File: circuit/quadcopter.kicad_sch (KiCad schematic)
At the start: 110 parts, among them J1 Conn_01x01_Female, J10 Conn_01x01_Female, J13 Conn_01x01_Female, J15 Conn_01x01_Female, J16 Conn_01x01_Female, J17 Conn_01x01_Female, J18 USB_C_Receptacle_USB2.0, J19 Conn_01x08_Male, J2 Conn_01x01_Female, J21 Conn_01x01_Female, J22 Conn_01x01_Female, J23 Conn_01x01_Female, J24 Conn_01x01_Female, J25 Conn_01x01_Female, J26 Conn_01x01_Female, J28 Conn_01x01_Female, J29 Conn_01x01_Female, J3 Conn_01x01_Female, J30 Conn_01x01_Female, J31 Conn_01x01_Female, J32 Conn_01x01_Female, J33 Conn_01x01_Female, J34 Conn_01x01_Female, J37 Conn_01x01_Female, J4 Conn_01x01_Female, J40 Conn_01x01_Female, J41 Conn_01x01_Female, J42 Conn_01x01_Female, J43 Conn_01x01_Female, J44 Conn_01x01_Female, J45 Conn_01x01_Female, J46 Conn_01x01_Female, J47 Conn_01x01_Female, J48 Conn_01x01_Female, J49 Conn_01x01_Female, J5 Conn_Coaxial, J50 Conn_01x01_Female, J6 Conn_01x06_Male, J7 Conn_01x01_Female, J8 Conn_01x01_Female, J9 Conn_01x01_Female, Q1 AO3400A, SW1 SW_DIP_x01, U1 STM32G431CBU6, U2 ICM-42605, U3 DPS310, U4 3V3, U5 5V out, 30V max, U6 2450FM07D0034T, U7 W25Q80DVUXIE TR, U8 SX1281, Y1 16M, Y2 52Mhz, 12pF

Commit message: More work on routing
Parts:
- U7: value W25Q80DVUXIE TR -> W25Q80DVUXIE TR (16M)
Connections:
- net +3V3: no longer C19.2, C26.1, C28.2, L3.1, U8.1 (VR_PA), U8.2 (VDD_IN)
- net V_DCC: now also C26.1, C28.2, L3.1, U8.2 (VDD_IN)
- new net: C19.2, U8.1 (VR_PA)
- no-connect marks 7 -> 9
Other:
- note added: "10v reg for cam and vtx? Would allow for 8S batteries, if you also up max voltage on a few other parts"
- note added: "Example full buzzer circuit. Not on PCB or BOM."
- note added: "SWD connections for ST-Link debugging and flashing"
- note added: "Todo: TVS diode across battery?"
- note removed: "10v reg for cam and vtx?"
- note removed: "Example full buzzer circuit. Not on BOM!"
- note removed: "todo: Higher capacity flash"
- moved on the sheet: C2, C23, C5, J16, J17, J32, J33, J40, J41, J42, J43, J44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

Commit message: Power section redid, including 10v reg added
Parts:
- removed U5: 5V out, 30V max, Package_TO_SOT_SMD:SOT-89-3, symbol Regulator_Linear:HT75xx-1-SOT89
- added C20: 22uF 25V, Capacitor_SMD:C_0805_2012Metric, symbol Device:C
- added C21: 10nF 50V, Capacitor_SMD:C_0402_1005Metric, symbol Device:C
- added C22: 2.2u, Capacitor_SMD:C_0402_1005Metric, symbol Device:C
- added D4: SOD24-7 26V breakdown, Diode_SMD:D_SOD-323, symbol Device:D
- added D5: 40v 1A B5819WS, Diode_SMD:D_SOD-323, symbol Device:D
- added L4: 22u 900mA, Anyleaf_Shared:SMNR4020 inductor, symbol Device:L
- added R7: 3.3K, Resistor_SMD:R_0402_1005Metric, symbol Device:R
- added R8: 300, Resistor_SMD:R_0402_1005Metric, symbol Device:R
- added U5: EUP3458 1.2A, 30V max input, adj output, Package_TO_SOT_SMD:TSOT-23-6, symbol Regulator_Switching:AAT1217ICA-1.2
- added U9: 5v, 500mA, Package_TO_SOT_SMD:TSOT-23-5, symbol water_monitor-rescue:MCP1802-3.3-Anyleaf_shared
- C15: value 10uF 10V -> 1u 50V; LCSC C19702 -> C15849
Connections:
- net +5V: now also D5.1 (K); no longer D2.1 (K)
- net +BATT: now also D4.1 (K), U5.4 (EN), U5.5 (IN); no longer C27.2, J25.1 (Pin_1), J6.6 (Pin_6), L2.2
- net BAT_IN: now also D4.2 (A); no longer L2.1
- net GND: now also D2.2 (A), C20.2, C22.1, R8.1, U5.2 (GND), U9.2 (GND)
- net +10V: now reaches C15.2
- net +10V: now also J25.1 (Pin_1), J6.6 (Pin_6), C20.1, L4.1, R7.2, U9.1 (VIN), U9.3 (~{SHDN}); no longer D2.2 (A)
- new net: C21.1, U5.1 (BS)
- new net: C21.2, D2.1 (K), L4.2, U5.6 (SW)
- new net: C22.2, C27.2, L2.1, U9.5 (VOUT)
- new net: D5.2 (A), L2.2
- new net: R7.1, R8.2, U5.3 (FB)
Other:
- note added: "3.3k and 300 lead to 9.6V output"
- note added: "Analog filtering on the 5V line. We can use a smaller inductor here, than if it were on the 10k line that needs to handle current to the cam/Vtx"
- note added: "Calculated inductor value, for 25.2v in, 9.6vout, 30% ripple, and 1A current: 16.5uH"
- note added: "Note: Voltage range of CADDX vista DJI: 7.4 - 26.4V HDzero: Racev2: 7-26V Hdzero freestyle: 7-17V"
- note added: "See regulator DS for info on how to set resistances and capacitances"
- note added: "TVS diode to block transient voltage spikes"
- note added: "Using Diatone pinout, since it's perhaps the most popular (2022) Note that this places the battery line next to the signal pins; Batt -> Gnd -> current/uart -> motor may be a better layout."
- note added: "V_out = 0.8V * (R1 + R2)/R2"
- note added: "todo: Bigger flash, on back side?"
- note removed: "10v reg for cam and vtx? Would allow for 8S batteries, if you also up max voltage on a few other parts"
- note removed: "Battery cicrcuit that includes a LC lowpass filter, to reduce noise from the ESC."
- note removed: "Note: Voltage range of CADDX vista DJI: 7.4 - 26.4V HDzero: Racev2: 7-26V Hdzero freestyle: 7-17V max (4S!)"
- note removed: "See https://github.com/ExpressLRS/ExpressLRS-Hardware/tree/master/PCB/2400MHz/RX_Nano for a ELRS example"
- note removed: "Todo: TVS diode across battery?"
- note removed: "Using Diatone pinout, since it's perhaps the most popular (2022)"
- note removed: "todo: Check max v on inductor"
- moved on the sheet: C14, C27, C7, C8, D2, D3, J10, J13, J19, J21, J22, J23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

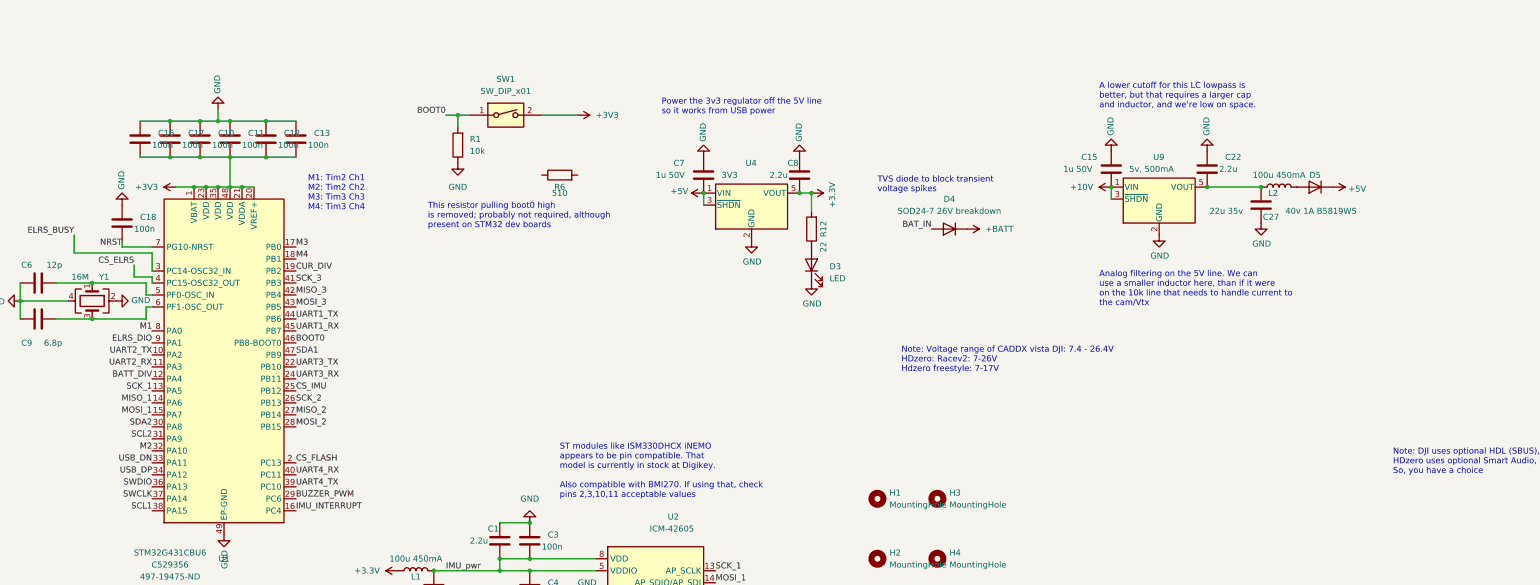
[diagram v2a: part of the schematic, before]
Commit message: More work on translating ELRS receiver code
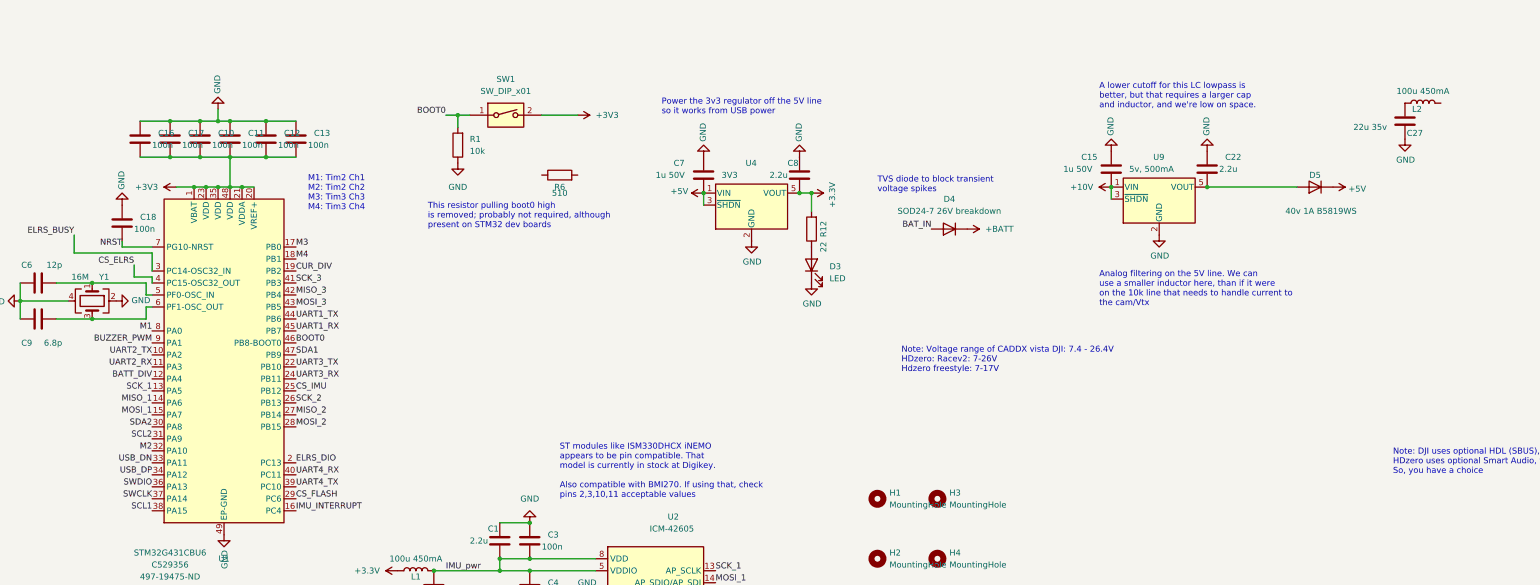
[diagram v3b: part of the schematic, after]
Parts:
- C27, L2: now left out of the parts list
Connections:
- net BUZZER_PWM: now also U1.9 (PA1); no longer U1.29 (PC6)
- net CS_FLASH: now also U1.29 (PC6); no longer U1.2 (PC13)
- net ELRS_DIO: now also U1.2 (PC13); no longer U1.9 (PA1)
- net at C22.2, U9.5 (VOUT): now also D5.2 (A); no longer C27.2, L2.1
- net at L2.2: no longer D5.2 (A)
- new net: C27.2, L2.1
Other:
- moved on the sheet: C27, L2
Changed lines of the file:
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@@
   (junction (at 54.61 336.55) (diameter 0) (color 0 0 0 0)
   )
-  (junction (at 347.98 48.26) (diameter 0) (color 0 0 0 0)
-  )
   (junction (at 193.04 129.54) (diameter 0) (color 0 0 0 0)
   )
@@
     (stroke (width 0) (type default) (color 0 0 0 0))
   )
-  (wire (pts (xy 336.55 48.26) (xy 347.98 48.26))
+  (wire (pts (xy 336.55 48.26) (xy 355.6 48.26))
     (stroke (width 0) (type default) (color 0 0 0 0))
   )
@@
     (effects (font (size 1.27 1.27)) (justify left bottom))
   )
-  (label "BUZZER_PWM" (at 143.51 114.3 0)
-    (effects (font (size 1.27 1.27)) (justify left bottom))
+  (label "BUZZER_PWM" (at 113.03 81.28 180)
+    (effects (font (size 1.27 1.27)) (justify right bottom))
   )
   (label "MOSI_3" (at 78.74 303.53 0)
@@
     (effects (font (size 1.27 1.27)) (justify right bottom))
   )
-  (label "CS_FLASH" (at 143.51 106.68 0)
+  (label "CS_FLASH" (at 143.51 114.3 0)
     (effects (font (size 1.27 1.27)) (justify left bottom))
   )
@@
     (effects (font (size 1.27 1.27)) (justify left bottom))
   )
-  (label "ELRS_DIO" (at 113.03 81.28 180)
-    (effects (font (size 1.27 1.27)) (justify right bottom))
+  (label "ELRS_DIO" (at 143.51 106.68 0)
+    (effects (font (size 1.27 1.27)) (justify left bottom))
   )
   (label "CS_ELRS" (at 109.22 64.77 180)
@@
     (pin "1")
   )
-  (symbol (lib_id "power:GND") (at 347.98 55.88 0) (unit 1)
+  (symbol (lib_id "power:GND") (at 378.46 38.1 0) (unit 1)
     (in_bom yes) (on_board yes)
-    (property "Reference" "#PWR?" (id 0) (at 347.98 62.23 0)
+    (property "Reference" "#PWR0125" (id 0) (at 378.46 44.45 0)
       (effects (font (size 1.27 1.27)) hide)
     )
-    (property "Value" "GND" (id 1) (at 348.107 60.2742 0))
-    (property "Footprint" "" (id 2) (at 347.98 55.88 0)
+    (property "Value" "GND" (id 1) (at 378.587 42.4942 0))
+    (property "Footprint" "" (id 2) (at 378.46 38.1 0)
       (effects (font (size 1.27 1.27)) hide)
     )
-    (property "Datasheet" "" (id 3) (at 347.98 55.88 0)
+    (property "Datasheet" "" (id 3) (at 378.46 38.1 0)
       (effects (font (size 1.27 1.27)) hide)
     )
@@
     (pin "2")
   )
-  (symbol (lib_id "Device:L") (at 351.79 48.26 90) (unit 1)
-    (in_bom yes) (on_board yes)
-    (property "Reference" "L2" (id 0) (at 350.52 49.53 90))
-    (property "Value" "100u 450mA" (id 1) (at 351.79 45.72 90))
-    (property "Footprint" "Anyleaf_Shared:SMNR4020 inductor" (id 2) (at 351.79 48.26 0)
+  (symbol (lib_id "Device:L") (at 382.27 30.48 90) (unit 1)
+    (in_bom no) (on_board no)
+    (property "Reference" "L2" (id 0) (at 381 31.75 90))
+    (property "Value" "100u 450mA" (id 1) (at 382.27 27.94 90))
+    (property "Footprint" "Anyleaf_Shared:SMNR4020 inductor" (id 2) (at 382.27 30.48 0)
       (effects (font (size 1.27 1.27)) hide)
     )
-    (property "Datasheet" "~" (id 3) (at 351.79 48.26 0)
+    (property "Datasheet" "~" (id 3) (at 382.27 30.48 0)
       (effects (font (size 1.27 1.27)) hide)
     )
-    (property "LCSC" "C467068" (id 4) (at 351.79 48.26 90)
+    (property "LCSC" "C467068" (id 4) (at 382.27 30.48 90)
       (effects (font (size 1.27 1.27)) hide)
     )
@@
     (pin "2")
   )
-  (symbol (lib_id "Device:C") (at 347.98 52.07 180) (unit 1)
-    (in_bom yes) (on_board yes)
-    (property "Reference" "C27" (id 0) (at 351.79 54.61 0)
+  (symbol (lib_id "Device:C") (at 378.46 34.29 180) (unit 1)
+    (in_bom no) (on_board no)
+    (property "Reference" "C27" (id 0) (at 382.27 36.83 0)
       (effects (font (size 1.27 1.27)) (justify left))
     )
-    (property "Value" "22u 35v" (id 1) (at 344.17 53.34 0)
+    (property "Value" "22u 35v" (id 1) (at 374.65 35.56 0)
       (effects (font (size 1.27 1.27)) (justify left))
     )
-    (property "Footprint" "Capacitor_SMD:C_0805_2012Metric" (id 2) (at 347.0148 48.26 0)
+    (property "Footprint" "Capacitor_SMD:C_0805_2012Metric" (id 2) (at 377.4948 30.48 0)
       (effects (font (size 1.27 1.27)) hide)
     )
-    (property "Datasheet" "~" (id 3) (at 347.98 52.07 0)
+    (property "Datasheet" "~" (id 3) (at 378.46 34.29 0)
       (effects (font (size 1.27 1.27)) hide)
     )
-    (property "LCSC" "C338080" (id 4) (at 347.98 52.07 0)
+    (property "LCSC" "C338080" (id 4) (at 378.46 34.29 0)
       (effects (font (size 1.27 1.27)) hide)
     )
@@
       (reference "#PWR0124") (unit 1) (value "GND") (footprint "")
     )
+    (path "/4cd6c931-bf25-4c72-8d1d-bb9bbbcd4add"
+      (reference "#PWR0125") (unit 1) (value "GND") (footprint "")
+    )
     (path "/76e20596-6bdb-42cd-a1dc-9b44805b2ea2"
       (reference "#PWR0126") (unit 1) (value "GND") (footprint "")
@@
       (reference "#PWR0180") (unit 1) (value "GND") (footprint "")
     )
-    (path "/4cd6c931-bf25-4c72-8d1d-bb9bbbcd4add"
-      (reference "#PWR?") (unit 1) (value "GND") (footprint "")
-    )
     (path "/4392ec2f-3eec-47ea-978d-f1725d990b74"

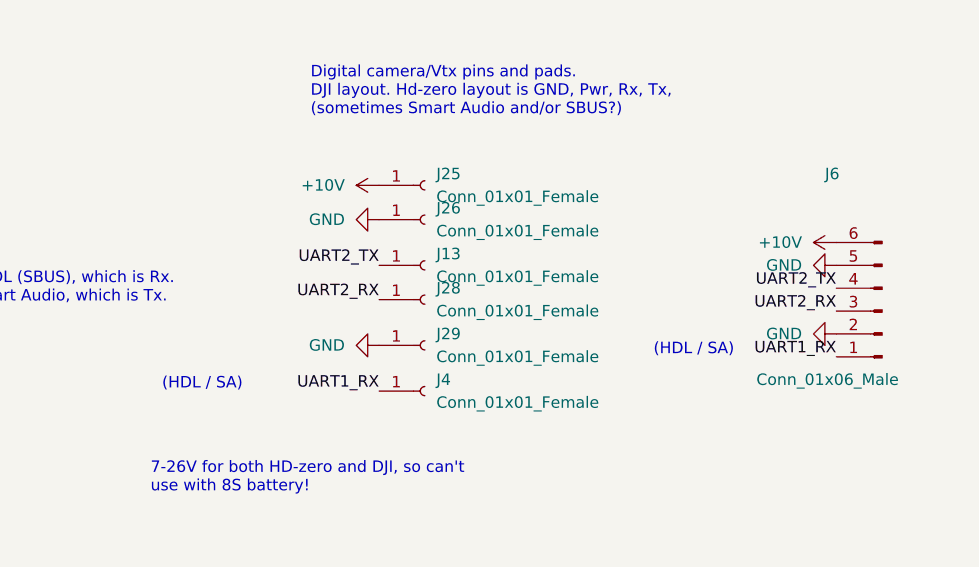
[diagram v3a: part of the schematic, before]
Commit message: Added list of ESC and VtX pinouts. Tweaks to IMU dma code
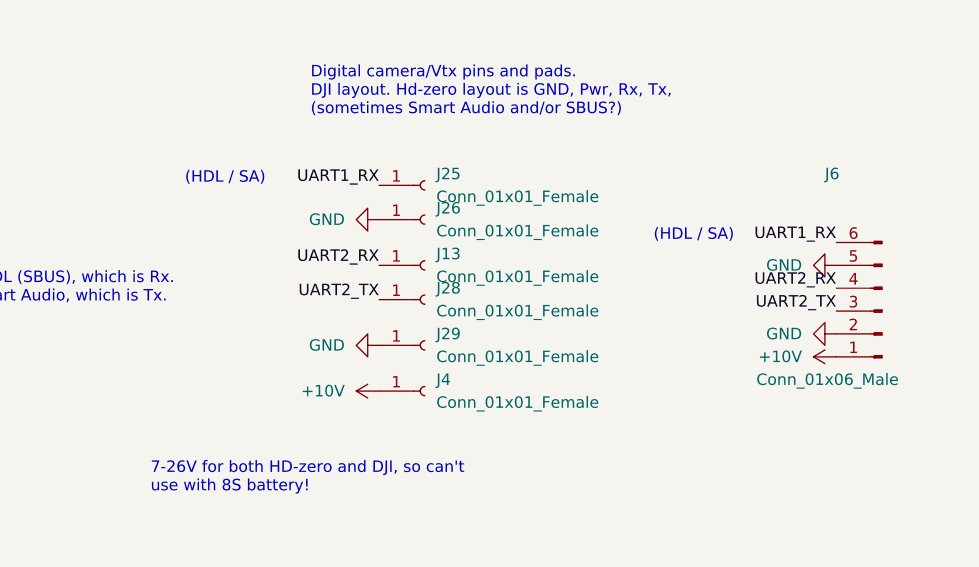
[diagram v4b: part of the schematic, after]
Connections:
- net +10V: now also J4.1 (Pin_1), J6.1 (Pin_1); no longer J25.1 (Pin_1), J6.6 (Pin_6)
- net UART1_RX: now also J25.1 (Pin_1), J6.6 (Pin_6); no longer J4.1 (Pin_1), J6.1 (Pin_1)
- net UART2_RX: now also J13.1 (Pin_1), J6.4 (Pin_4); no longer J28.1 (Pin_1), J6.3 (Pin_3)
- net UART2_TX: now also J28.1 (Pin_1), J6.3 (Pin_3); no longer J13.1 (Pin_1), J6.4 (Pin_4)
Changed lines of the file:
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@@
     (stroke (width 0) (type default) (color 0 0 0 0))
   )
-  (text "(HDL / SA)" (at 471.17 113.03 0)
+  (text "(HDL / SA)" (at 471.17 100.33 0)
     (effects (font (size 1.27 1.27)) (justify left bottom))
   )
@@
     (effects (font (size 1.27 1.27)) (justify left bottom))
   )
-  (text "(HDL / SA)" (at 416.56 116.84 0)
+  (text "(HDL / SA)" (at 419.1 93.98 0)
     (effects (font (size 1.27 1.27)) (justify left bottom))
   )
@@
     (effects (font (size 1.27 1.27)) (justify left bottom))
   )
-  (label "UART2_RX" (at 491.49 107.95 180)
+  (label "UART2_RX" (at 491.49 105.41 180)
     (effects (font (size 1.27 1.27)) (justify right bottom))
   )
@@
     (effects (font (size 1.27 1.27)) (justify left bottom))
   )
-  (label "UART2_TX" (at 491.49 105.41 180)
+  (label "UART2_TX" (at 491.49 107.95 180)
     (effects (font (size 1.27 1.27)) (justify right bottom))
   )
@@
     (effects (font (size 1.27 1.27)) (justify right bottom))
   )
-  (label "UART2_RX" (at 440.69 106.68 180)
+  (label "UART2_RX" (at 440.69 102.87 180)
     (effects (font (size 1.27 1.27)) (justify right bottom))
   )
@@
     (effects (font (size 1.27 1.27)) (justify left bottom))
   )
-  (label "UART2_TX" (at 440.69 102.87 180)
+  (label "UART2_TX" (at 440.69 106.68 180)
     (effects (font (size 1.27 1.27)) (justify right bottom))
   )
@@
     (effects (font (size 1.27 1.27)) (justify right bottom))
   )
-  (label "UART1_RX" (at 440.69 116.84 180)
+  (label "UART1_RX" (at 440.69 93.98 180)
     (effects (font (size 1.27 1.27)) (justify right bottom))
   )
-  (label "UART1_RX" (at 491.49 113.03 180)
+  (label "UART1_RX" (at 491.49 100.33 180)
     (effects (font (size 1.27 1.27)) (justify right bottom))
   )
@@
     (pin "1")
   )
-  (symbol (lib_id "power:+10V") (at 491.49 100.33 90) (unit 1)
+  (symbol (lib_id "power:+10V") (at 491.49 113.03 90) (unit 1)
     (in_bom yes) (on_board yes) (fields_autoplaced)
-    (property "Reference" "#PWR0147" (id 0) (at 495.3 100.33 0)
+    (property "Reference" "#PWR0147" (id 0) (at 495.3 113.03 0)
       (effects (font (size 1.27 1.27)) hide)
     )
-    (property "Value" "+10V" (id 1) (at 487.68 100.3299 90)
+    (property "Value" "+10V" (id 1) (at 487.68 113.0299 90)
       (effects (font (size 1.27 1.27)) (justify left))
     )
-    (property "Footprint" "" (id 2) (at 491.49 100.33 0)
+    (property "Footprint" "" (id 2) (at 491.49 113.03 0)
       (effects (font (size 1.27 1.27)) hide)
     )
-    (property "Datasheet" "" (id 3) (at 491.49 100.33 0)
+    (property "Datasheet" "" (id 3) (at 491.49 113.03 0)
       (effects (font (size 1.27 1.27)) hide)
     )
@@
     (pin "6")
   )
-  (symbol (lib_id "power:+10V") (at 440.69 93.98 90) (unit 1)
+  (symbol (lib_id "power:+10V") (at 440.69 116.84 90) (unit 1)
     (in_bom yes) (on_board yes) (fields_autoplaced)
-    (property "Reference" "#PWR0111" (id 0) (at 444.5 93.98 0)
+    (property "Reference" "#PWR0111" (id 0) (at 444.5 116.84 0)
       (effects (font (size 1.27 1.27)) hide)
     )
-    (property "Value" "+10V" (id 1) (at 436.88 93.9799 90)
+    (property "Value" "+10V" (id 1) (at 436.88 116.8399 90)
       (effects (font (size 1.27 1.27)) (justify left))
     )
-    (property "Footprint" "" (id 2) (at 440.69 93.98 0)
+    (property "Footprint" "" (id 2) (at 440.69 116.84 0)
       (effects (font (size 1.27 1.27)) hide)
     )
-    (property "Datasheet" "" (id 3) (at 440.69 93.98 0)
+    (property "Datasheet" "" (id 3) (at 440.69 116.84 0)
       (effects (font (size 1.27 1.27)) hide)
     )
